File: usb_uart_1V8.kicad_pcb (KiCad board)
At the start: 2 copper layers, 15 parts, among them J1 USB_B_Micro, J2 Conn_01x04_Pin, J3 Conn_01x04_Pin, U1 FT232RNL

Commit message: [UPG] pcb
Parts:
- added C5: 100nF, Capacitor_SMD:C_0402_1005Metric, F.Cu at (132.0, 133.0)
- added C6: 100nF, Capacitor_SMD:C_0402_1005Metric, F.Cu at (133.7, 133.0)
- added D4: XL-1608SURC-06FJ, LED_SMD:LED_0603_1608Metric, F.Cu at (132.3, 121.3)
- added Q1: MMBT3904, Package_TO_SOT_SMD:SOT-23, F.Cu at (136.9, 122.8)
- added R4: 680, Resistor_SMD:R_0402_1005Metric, F.Cu at (137.2, 126.6)
- added R5: 47k, Resistor_SMD:R_0402_1005Metric, F.Cu at (132.8, 124.3)
- added R6: 4k7, Resistor_SMD:R_0402_1005Metric, F.Cu at (140.2, 135.7)
- added R7: 4k7, Resistor_SMD:R_0402_1005Metric, F.Cu at (140.2, 130.4)
- added U3: SN74LVC1T45DBV, Package_TO_SOT_SMD:SOT-23-6, F.Cu at (137.3, 135.7)
- added U4: SN74LVC1T45DBV, Package_TO_SOT_SMD:SOT-23-6, F.Cu at (137.3, 130.4)
- R2, R3: value 1k2 -> 270
- moved R2 97.7 mm to (151.9, 136.5), turned to 0 degrees
- moved U1 96.6 mm to (149.9, 129.2)
- moved C1 95.3 mm to (155.4, 135.8), turned to 90 degrees
- moved C4 94.4 mm to (133.0, 128.4), turned to 90 degrees
- moved C3 94.3 mm to (157.5, 136.3)
- moved R3 93.2 mm to (152.0, 121.8), turned to 180 degrees
- moved C2 93.1 mm to (162.1, 136.3)
- moved R1 92.9 mm to (161.3, 123.3)
- moved D2 92.9 mm to (148.1, 136.5), turned to 180 degrees
- moved FB1 91.2 mm to (157.7, 132.0), turned to 90 degrees
- moved J1 91.1 mm to (163.1, 129.2)
- moved J3 90.5 mm to (128.0, 125.4)
- moved D1 90.2 mm to (158.2, 124.3)
- moved J2 89.0 mm to (120.9, 125.4)
- moved D3 87.1 mm to (148.1, 121.8), turned to 180 degrees
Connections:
- D2 pad 2: VBUS -> +3V3
- D3 pad 2: VBUS -> +3V3
- U1 pad 1: /TX -> /TX_3V3
- U1 pad 4: VCC_TTL -> +3V3
- U1 pad 5: /RX -> /RX_3V3
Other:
- board outline added: 47.7 x 21 mm
- board text added: "RX"
- board text added: "TX"
- board text added: "VBUS"
- board text added: "VCC"
- board text added: "VCC 1.8~5V"

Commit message: [UPG] almost finished PCB
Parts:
- moved R4 5.21 mm to (136.9, 121.4)
- moved FB1 3.69 mm to (158.0, 128.3)
- moved Q1 2.71 mm to (136.4, 125.5)
- moved D4 0.13 mm to (132.3, 121.4)
- turned R3 to 0 degrees
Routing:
- net +3V3: track 0.00 -> 52.4 mm
- net GND: track 0.00 -> 40.9 mm, vias 0 -> 8
- net VBUS: track 0.00 -> 37.6 mm, vias 0 -> 2
- net /TX: track 0.00 -> 36.3 mm, vias 0 -> 1
- net /RX: track 0.00 -> 21.1 mm
- net /RX_3V3: track 0.00 -> 18.1 mm
- net VCC_TTL: track 0.00 -> 16.3 mm, vias 0 -> 3
- net /TXL: track 0.00 -> 11.9 mm, vias 0 -> 2
- net /D+: track 0.00 -> 9.96 mm
- net /TX_3V3: track 0.00 -> 9.83 mm
- net /D-: track 0.00 -> 9.70 mm, vias 0 -> 2
- net /RXL: track 0.00 -> 9.44 mm
- net Net-(J1-VBUS): track 0.00 -> 6.22 mm, vias 0 -> 2
- net Net-(D4-K): track 0.00 -> 5.53 mm
- net Net-(Q1-C): track 0.00 -> 4.10 mm
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- added copper zone on F.Cu, net +3V3
- added copper zone on B.Cu, net GND
- added copper zone on F.Cu, net VBUS
- added copper zone on F.Cu, net VCC_TTL

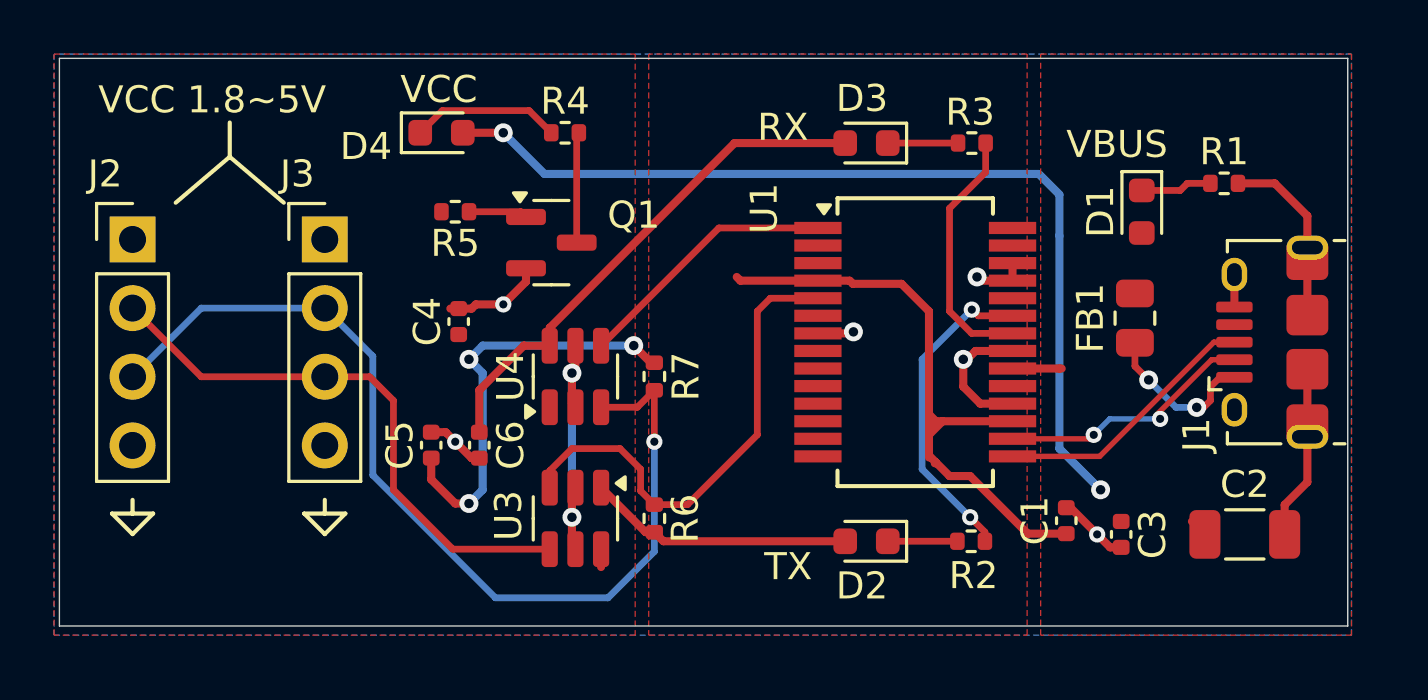
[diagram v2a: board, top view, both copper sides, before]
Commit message: [UPG] level shifter: 2 become 1
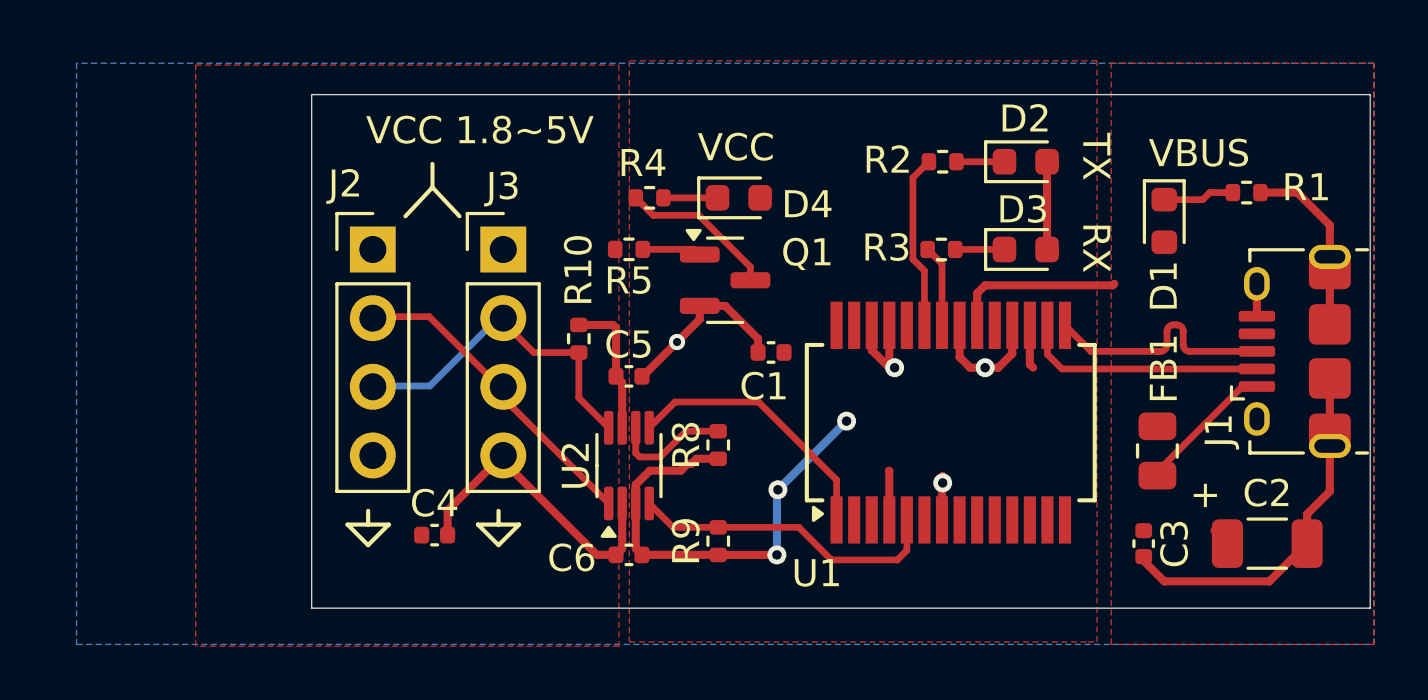
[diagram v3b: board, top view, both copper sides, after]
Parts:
- removed R6, R7: 4k7, Resistor_SMD:R_0402_1005Metric
- removed U3, U4: SN74LVC1T45DBV, Package_TO_SOT_SMD:SOT-23-6
- added G***: LOGO, usb_uart_1V8:delta_MC, B.Cu at (150.4, 129.0)
- added R10: 4k7, Resistor_SMD:R_0402_1005Metric, F.Cu at (137.4, 129.0)
- added R8: 4k7, Resistor_SMD:R_0402_1005Metric, F.Cu at (142.6, 133.0)
- added R9: 4k7, Resistor_SMD:R_0402_1005Metric, F.Cu at (142.6, 136.5)
- added U2: TXU0202DCU, Package_SO:VSSOP-8_2.3x2mm_P0.5mm, F.Cu at (139.3, 133.7)
- J2, J3: value Conn_01x04_Pin -> PZ254V-11-04P
- R4: value 680 -> 390
- moved D2 15.2 mm to (153.9, 122.5), turned to 0 degrees
- moved R2 14.1 mm to (150.9, 122.5), turned to 180 degrees
- moved C1 12.6 mm to (144.5, 129.5), turned to 180 degrees
- moved D4 11.3 mm to (143.3, 123.8)
- moved J2 8.90 mm to (129.8, 125.7)
- moved C4 7.95 mm to (132.1, 136.3), turned to 0 degrees
- moved C5 7.75 mm to (139.3, 130.4), turned to 0 degrees
- moved D3 7.09 mm to (153.9, 125.7), turned to 0 degrees
- moved C6 6.87 mm to (139.3, 137.0), turned to 180 degrees
- moved J3 6.61 mm to (134.6, 125.7)
- moved Q1 6.58 mm to (142.8, 126.9)
- moved R5 6.58 mm to (139.3, 125.7)
- moved FB1 4.98 mm to (158.8, 133.2)
- moved R3 4.09 mm to (150.8, 125.7), turned to 180 degrees
- moved R4 3.95 mm to (140.0, 123.8), turned to 180 degrees
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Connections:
- D4 pad 2: VBUS -> +3V3
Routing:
- net VBUS: track 37.6 -> 7.59 mm, vias 2 -> 0
- net +3V3: track 52.4 -> 23.9 mm, vias 0 -> 3
- net /TX: track 36.3 -> 12.5 mm, vias 1 -> 0
- net VCC_TTL: track 16.3 -> 5.30 mm, vias 3 -> 0
- net /RX: track 21.1 -> 11.8 mm
- net GND: track 40.9 -> 49.2 mm, vias 8 -> 4
- net /RXL: track 9.44 -> 3.03 mm
- net /RX_3V3: track 18.1 -> 11.7 mm
- net /TXL: track 11.9 -> 6.47 mm, vias 2 -> 0
- net Net-(U2-OE): track 0.00 -> 4.44 mm
- net Net-(D4-K): track 5.53 -> 2.00 mm
- net Net-(Q1-C): track 4.10 -> 5.79 mm
- net /D+: track 9.96 -> 9.01 mm
- net Net-(J1-VBUS): track 6.22 -> 5.41 mm, vias 2 -> 0
- net Net-(D2-K): track 2.58 -> 1.78 mm
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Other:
- board size 47.7 x 21 mm -> 39.2 x 19 mm
- board text added: "+"
- board text added: "USB/Uart v0.1"

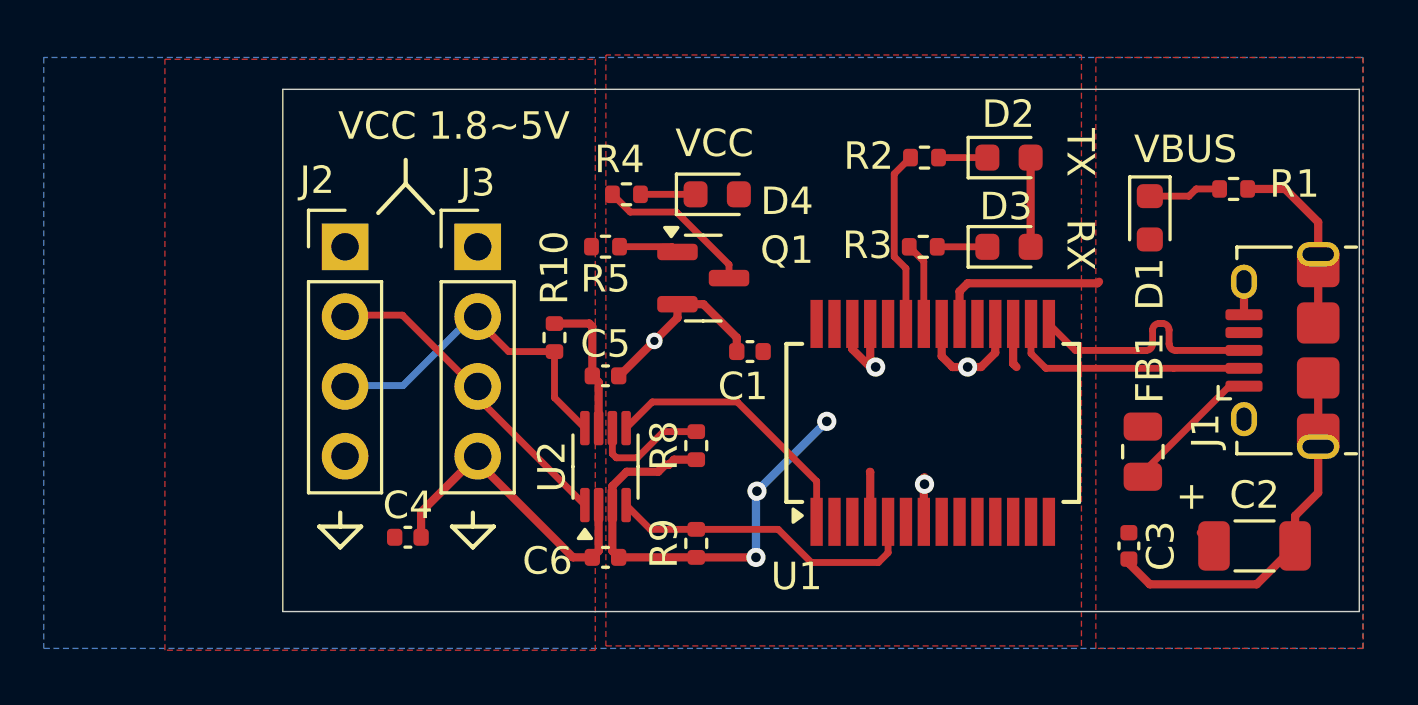
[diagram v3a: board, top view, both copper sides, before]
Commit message: [UPG] ver 0.4
- changed some values
- PN basic from JLCPCB
- reduced dimension
- changed some components, now are bigger, eg. 0402 -> 0603
- used handsolder footprint for fome resistor
- changed led (less efficient)
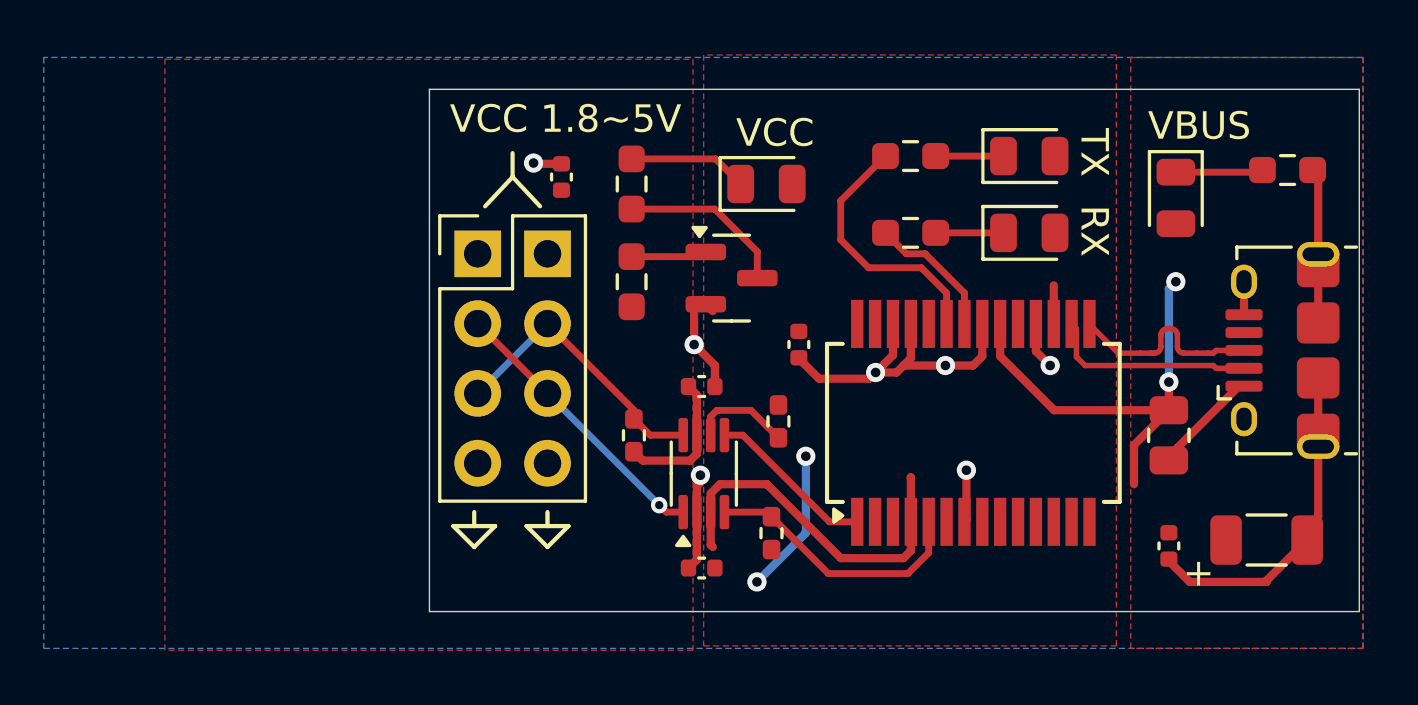
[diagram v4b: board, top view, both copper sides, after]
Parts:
- removed the C1 at (144.5, 129.5)
- removed J3: PZ254V-11-04P, Connector_PinHeader_2.54mm:PinHeader_1x04_P2.54mm_Vertical
- removed R10: 4k7, Resistor_SMD:R_0402_1005Metric
- removed the R8 at (142.6, 133.0)
- added C3: 100nF, Capacitor_SMD:C_0402_1005Metric, F.Cu at (146.3, 129.3)
- added G***: LOGO, usb_uart_1V8:open_hw, B.Cu at (160.5, 123.4)
- added G***: LOGO, usb_uart_1V8:kicad_nagative, B.Cu at (141.5, 127.0)
- added R5: 10k, Resistor_SMD:R_0402_1005Metric_Pad0.72x0.64mm_HandSolder, F.Cu at (145.6, 132.1)
- added R6: 10k, Resistor_SMD:R_0402_1005Metric_Pad0.72x0.64mm_HandSolder, F.Cu at (140.3, 132.6)
- D1, D2, D3, D4: value XL-1608SURC-06FJ -> NCD0805R1; footprint LED_SMD:LED_0603_1608Metric -> LED_SMD:LED_0805_2012Metric
- FB1: value HCB1608KF-471T20 -> GZ2012D601TF
- J2: value PZ254V-11-04P -> Conn_02x04_Odd_Even; footprint Connector_PinHeader_2.54mm:PinHeader_1x04_P2.54mm_Vertical -> Connector_PinHeader_2.54mm:PinHeader_2x04_P2.54mm_Vertical
- R1: value 1k2 -> 1k5; footprint Resistor_SMD:R_0402_1005Metric -> Resistor_SMD:R_0603_1608Metric_Pad0.98x0.95mm_HandSolder
- R2, R3: footprint Resistor_SMD:R_0402_1005Metric -> Resistor_SMD:R_0603_1608Metric_Pad0.98x0.95mm_HandSolder
- R4: renamed from R9; value 4k7 -> 10k; footprint Resistor_SMD:R_0402_1005Metric -> Resistor_SMD:R_0402_1005Metric_Pad0.72x0.64mm_HandSolder
- R7: renamed from R4; value 390 -> 470; footprint Resistor_SMD:R_0402_1005Metric -> Resistor_SMD:R_0603_1608Metric_Pad0.98x0.95mm_HandSolder
- R8: renamed from R5; footprint Resistor_SMD:R_0402_1005Metric -> Resistor_SMD:R_0603_1608Metric_Pad0.98x0.95mm_HandSolder
- moved C6 13.9 mm to (137.7, 123.2), turned to 90 degrees
- moved C4 10.7 mm to (142.8, 137.4), turned to 180 degrees
- moved J2 4.83 mm to (134.6, 126.0)
- moved U2 3.59 mm to (142.8, 134.0)
- moved C5 3.52 mm to (142.8, 130.8)
- moved G*** 3.14 mm to (153.4, 129.8), turned to 90 degrees
- moved R4 2.76 mm to (145.3, 136.1)
- moved R1 2.08 mm to (164.1, 122.9)
- moved D4 1.83 mm to (145.1, 123.4)
- moved R8 1.59 mm to (140.2, 127.0), turned to -90 degrees
- moved U1 1.48 mm to (152.7, 132.1)
- moved C1 1.45 mm to (159.8, 136.6)
- moved D1 1.19 mm to (160.0, 124.0)
- moved FB1 1.12 mm to (159.8, 132.6)
- moved Q1 1.03 mm to (143.9, 126.9)
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- renumbered C3 to C1
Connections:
- C4 pad 1: VCC_TTL -> +3V3
- C6 pad 1: +3V3 -> VCC_TTL
- J2 pad 2: /RX -> VCC_TTL
- J2 pad 3: /TX -> /RX
- J2 pad 4: GND -> /TX
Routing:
- net VBUS: track 7.59 -> 16.1 mm, vias 0 -> 2
- net GND: track 49.2 -> 42.2 mm, vias 4 -> 7
- net +3V3: track 23.9 -> 20.0 mm, vias 3 -> 2
- net /TX_3V3: track 10.00 -> 6.14 mm
- net /TXL: track 6.47 -> 9.50 mm
- net Net-(D4-K): track 2.00 -> 4.34 mm
- net /TX: track 12.5 -> 10.4 mm
- net /RXL: track 3.03 -> 4.91 mm
- net /RX_3V3: track 11.7 -> 9.80 mm
- net /D+: track 9.01 -> 7.45 mm
- net /D-: track 9.05 -> 7.54 mm
- net Net-(J1-VBUS): track 5.41 -> 3.94 mm
- net /RX: track 11.8 -> 10.3 mm, vias 0 -> 1
- net Net-(U2-OE): track 4.44 -> 3.65 mm
- net Net-(D2-K): track 1.78 -> 2.47 mm
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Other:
- board size 39.2 x 19 mm -> 33.8 x 19 mm
- board text added: "USB/Uart v${REVISION}"
- board text removed: "USB/Uart v0.1"

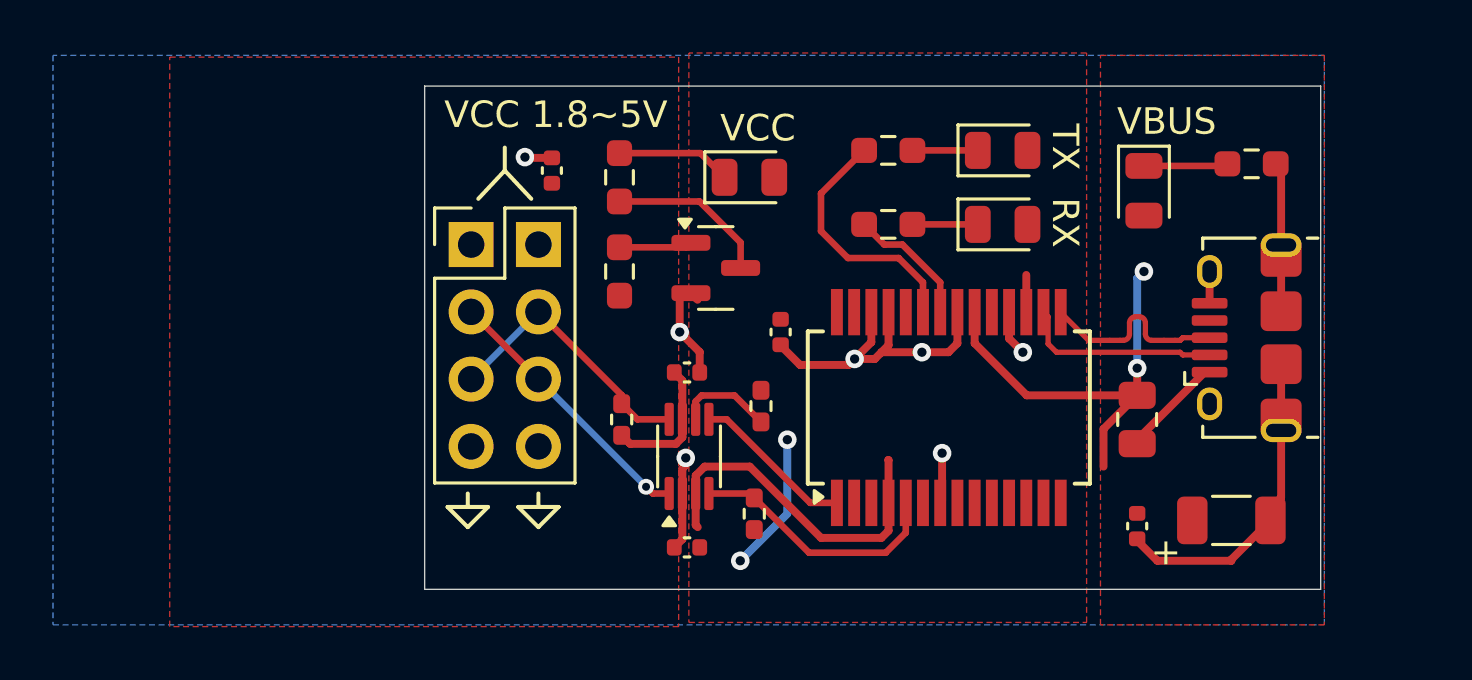
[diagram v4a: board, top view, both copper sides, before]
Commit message: [UPG] changed connector from micro-b to usb-c
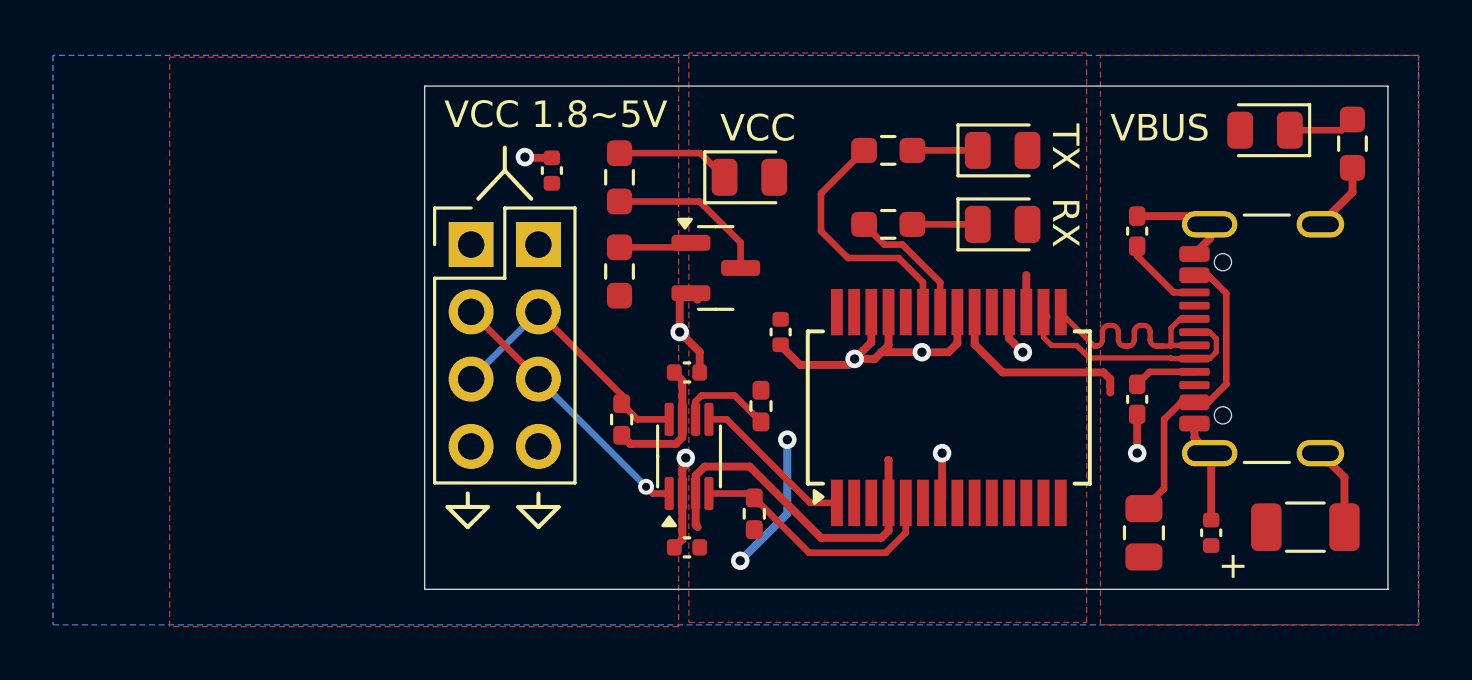
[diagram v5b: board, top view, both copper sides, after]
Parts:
- added R10: 5k1, Capacitor_SMD:C_0402_1005Metric_Pad0.74x0.62mm_HandSolder, F.Cu at (159.8, 125.5)
- added R9: 5k1, Capacitor_SMD:C_0402_1005Metric_Pad0.74x0.62mm_HandSolder, F.Cu at (159.8, 131.8)
- J1: value USB_B_Micro -> USB_C_Receptacle_USB2.0_16P; footprint Connector_USB:USB_Micro-B_Amphenol_10118194-0001LF_Horizontal -> Connector_USB:USB_C_Receptacle_GCT_USB4105-xx-A_16P_TopMnt_Horizontal
- moved G*** 7.94 mm to (165.6, 129.5)
- moved D1 5.11 mm to (164.6, 121.7), turned to 180 degrees
- moved FB1 4.29 mm to (160.0, 136.9), turned to -90 degrees
- moved R1 3.89 mm to (167.9, 122.2), turned to -90 degrees
- moved C1 2.81 mm to (162.6, 136.9), turned to 90 degrees
- moved C2 2.81 mm to (166.1, 136.7)
- moved J1 1.71 mm to (165.6, 129.5)
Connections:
- FB1 pad 1: Net-(J1-VBUS) -> Net-(FB1-Pad1)
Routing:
- net Net-(FB1-Pad1): track 0.00 -> 11.5 mm
- net VBUS: track 16.1 -> 7.39 mm, vias 2 -> 0
- net Net-(J1-VBUS): track 3.94 -> 0.00 mm
- net Net-(J1-CC2): track 0.00 -> 3.10 mm
- net GND: track 42.2 -> 39.5 mm, vias 7 -> 8
- net Net-(J1-CC1): track 0.00 -> 2.36 mm
- net /D+: track 7.45 -> 9.52 mm
- net /D-: track 7.54 -> 9.59 mm
- net Net-(D1-K): track 3.18 -> 2.53 mm
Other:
- board size 33.8 x 19 mm -> 36.4 x 19 mm
